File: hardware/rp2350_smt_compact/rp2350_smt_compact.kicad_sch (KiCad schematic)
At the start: 21 parts, among them J1 RP2350-Zero_SMT_Castellated(2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, J2 USB-A_Host(Neltron_5075AR-04-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, J3 RP2350-Zero_SMT_Castellated(2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, SW1 SS-12D00G3 SMD SPDT;Mute/GP28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, SW2 SS-12D00G3 SMD SPDT;Filter/GP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, SW3 SS-12D00G3 SMD SPDT;予備/GP27(フ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, SW4 SS-12D00G3 SMD SPDT;VBUS手動遮断(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, SW5 SS-12D00G3 SMD SPDT;サステイン/J3 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, SW6 PTS645 SMD 6x6 Tact;リセット/J3 G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, U1 TPS2051BDBVR_SOT23-5, U2 USBLC6-2SC6_SOT23-6_USB-A_ESD, U3 USBLC6-2SC6_SOT23-6_USB-C_fut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

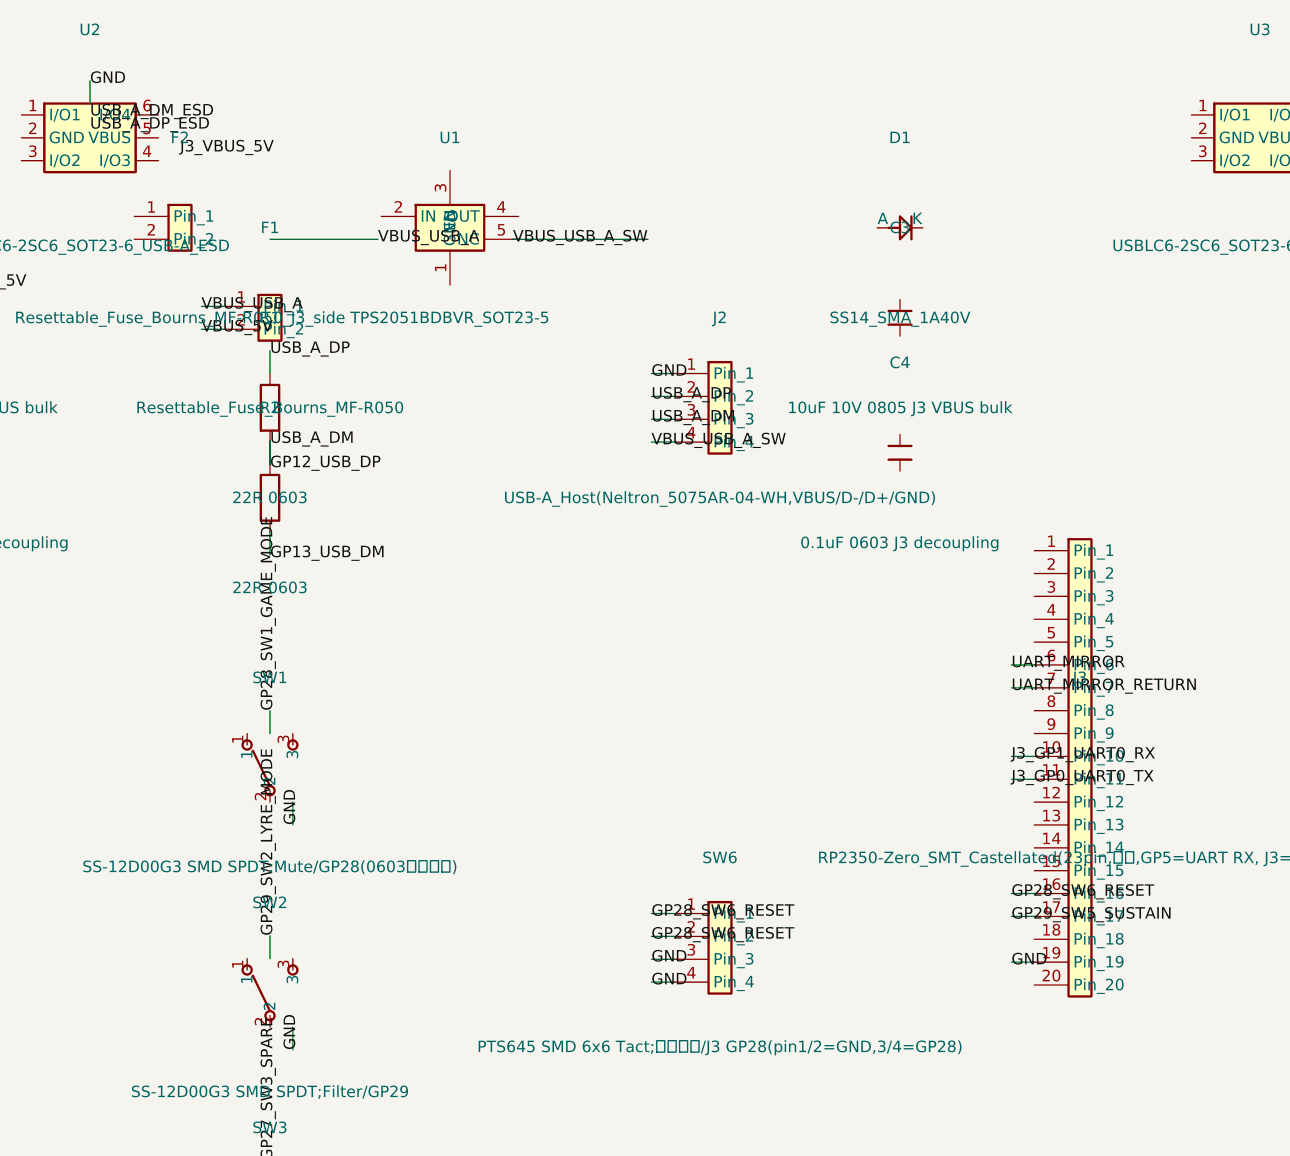
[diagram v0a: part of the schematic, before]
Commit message: review: fix SMT compact carrier inconsistencies
- kicad_pcb: R1/R2 を THT axial (through_hole, P10.16mm, drill0.8) から SMD 0603 (0.9x1.0mm, smd, gap0.8) に修正。pretty の R_0603 と一致、JLC Basic 手ハンダ可能パッケージに準拠。BOM 誤記 C25804(10k) を正しい 22Ω 0603 C22902 に整合
- kicad_pcb: J1/J3 を through_hole 円パッドから RP2350_Zero_SMT_23p_Castellated の正規 smd 矩形+NPTH 半穴定義 (attr smd) に置換。pretty と一致し Castellated Holes 指定を正しく表現。J3 5V を J3_VBUS_5V ネットに接続
- kicad_pcb: SW1-SW5 を THT 3pin (through_hole) から SMスライド SS-12D00G3 SMD 5pad ガルウィング (attr smd, 1.2x1.5mm, anchor 4/5 追加) に置換、SW6 を THT 4pin から PTS645 SMD 6x6 (4pad gull-wing) に置換。pretty と整合
- kicad_pcb: U1 TPS2051B SOT23-5 の未接続パッドにネット割当 (1=GND,2=VBUS_USB_A,3=GND(EN pull-down),4=VBUS_USB_A_SW)。D1/F2/C1-C4 の VBUS/GND ネットも補完
- kicad_sch: U1 EN と GND ピンの浮きを解消 (GND ラベルへ配線)、J3 5V→F2→D1 系と C3/C4 のデカップリングのラベル配線を追加 (いずれもホットプラグ突入対策)。U1 IN=VBUS_USB_A(F1後), OUT=VBUS_USB_A_SW(J2) の既定経路は変更なし
- pretty: 未使用 THT フットプリント 4種 (R_Axial_THT_P10.16mm, SW_SPDT_NKK_115643_Slide, SW_TACT_Akizuki_DTS63, RP2350_Zero_Header_23p) を削除。SMT試作の冗長性解消。残り13種は全て SMD/手ハンダ可能のみ
- bom.csv: R1/R2 の LCSC 誤記修正と備考追記

Edge.Cuts 50x35mm, 2チップ縦並び, 既存 carrier 非破壊, fp-lib-table 整合, USB4105 将来 QFN 言及は維持
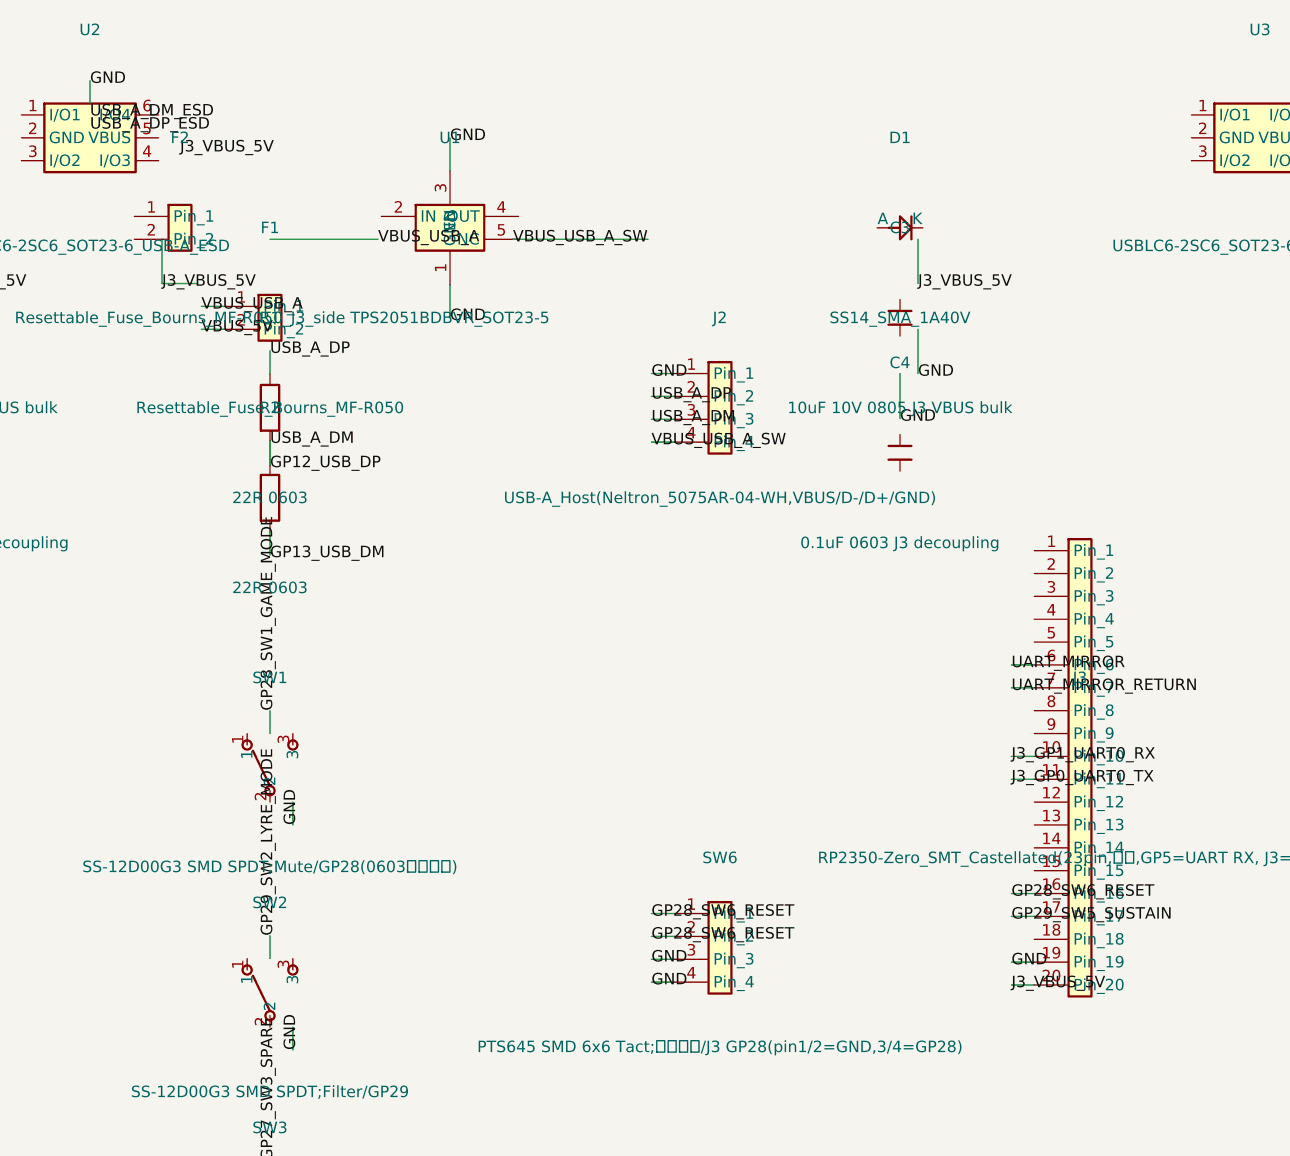
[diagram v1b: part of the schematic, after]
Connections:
- net GND: now also U1.1 (GND), U1.3 (EN)
- net J3_VBUS_5V: now also J3.20 (Pin_20)
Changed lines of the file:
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@@
   (label "USB_A_DP_ESD" (at 90 58.73 0) (effects (font (size 1.27 1.27)) (justify left)))
   (label "USB_A_DM_ESD" (at 90 57.27 0) (effects (font (size 1.27 1.27)) (justify left)))
+  (wire (pts (xy 130 76.35) (xy 130 80)) (stroke (width 0) (type default)))
+  (label "GND" (at 130 80 0) (effects (font (size 1.27 1.27)) (justify left)))
+  (wire (pts (xy 130 63.65) (xy 130 60)) (stroke (width 0) (type default)))
+  (label "GND" (at 130 60 0) (effects (font (size 1.27 1.27)) (justify left)))
+  (wire (pts (xy 194.92 154.13) (xy 192.38 154.13)) (stroke (width 0) (type default)))
+  (label "J3_VBUS_5V" (at 192.38 154.13 0) (effects (font (size 1.27 1.27)) (justify left)))
+  (wire (pts (xy 182 76.19) (xy 182 71.27)) (stroke (width 0) (type default)))
+  (label "J3_VBUS_5V" (at 182 76.19 0) (effects (font (size 1.27 1.27)) (justify left)))
+  (wire (pts (xy 182 86.19) (xy 182 81.27)) (stroke (width 0) (type default)))
+  (label "GND" (at 182 86.19 0) (effects (font (size 1.27 1.27)) (justify left)))
+  (wire (pts (xy 180 91.19) (xy 180 86.19)) (stroke (width 0) (type default)))
+  (label "GND" (at 180 91.19 0) (effects (font (size 1.27 1.27)) (justify left)))
+  (wire (pts (xy 98 76.19) (xy 98 71.27)) (stroke (width 0) (type default)))
+  (label "J3_VBUS_5V" (at 98 76.19 0) (effects (font (size 1.27 1.27)) (justify left)))
+  (wire (pts (xy 102 76.19) (xy 98 76.19)) (stroke (width 0) (type default)))
   (sheet_instances
     (path "/" (page "1"))

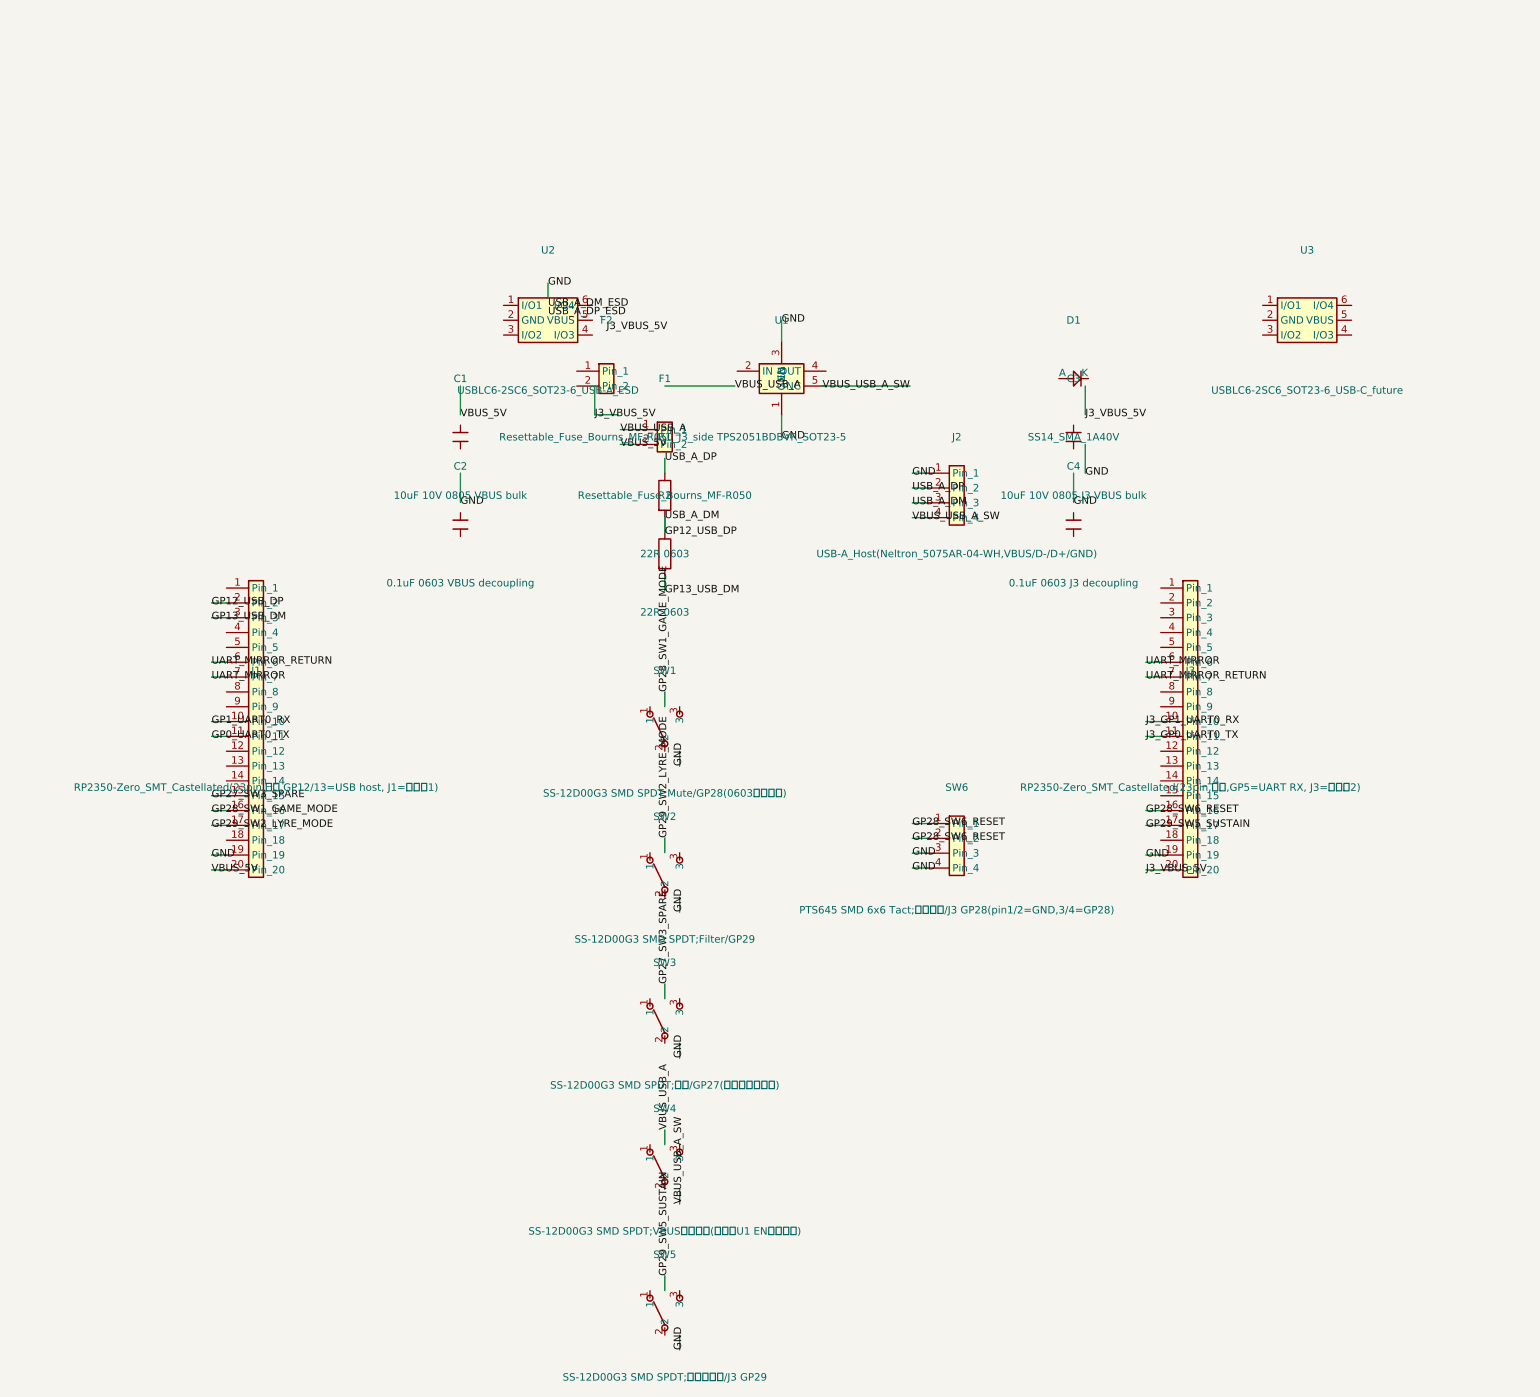
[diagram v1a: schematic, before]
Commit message: docs: kicad_sch清書 & PDF出力、一部pcb調整、配置確認用ドキュメント追加
- kicad_sch清書: 電源(5V→F1→U1 TPS2051B EN=GND→J2 VBUS / J3 5V→F2→D1 SS14)・USB(R1/R2 22R 0603差動90Ω)・ESD(U2/U3 USBLC6)・SW(SS-12D00/PTS645)をグリッド2.54mmに整列、シンボル間10mm以上、Valueを1.0mmフォントで重ならない位置に、ラベルはグローバルラベルで直交配線、重なり0でA4 1枚に収める。テキストで50×35mm構成を注記
- kicad_pcb: 配置確認用で配線除去を維持、Edge.Cuts 50×35mm内で J1(0,6)/J3(0,-6 180°)縦並び中心、J2(0,-14.2)底辺中央、U1(-4,-12.5)/D1(4,-12.5)とC1-4(-7/-3/3/7,-10)をVBUS沿い等間隔、SW1-4右側(16,9/4/-1/-6)・SW5/6左側(-16,-4/-16,9)等間隔、H1-4四隅、TP1(-14,0)中央でHと0.5mmクリアランス確保。シルクRefは読める位置、courtyard重なり0・はみ出し0をDRCで確認(残377件は配線未接続と半穴マスク起因で配置起因は0)
- PDF生成: kicad-cli sch export pdf → docs/smt_compact_sch.pdf(111K)、pcb export pdf(F.Cu/B.Cu/F.SilkS/B.SilkS/Edge.Cuts) → docs/smt_compact_pcb.pdf(36K)、pcb render top/3d → docs/smt_compact_top.png(59K)/smt_compact_3d.png(203K)
- 生成PDF/PNGを docs/ にコミットし FilesパネルからDL可能に
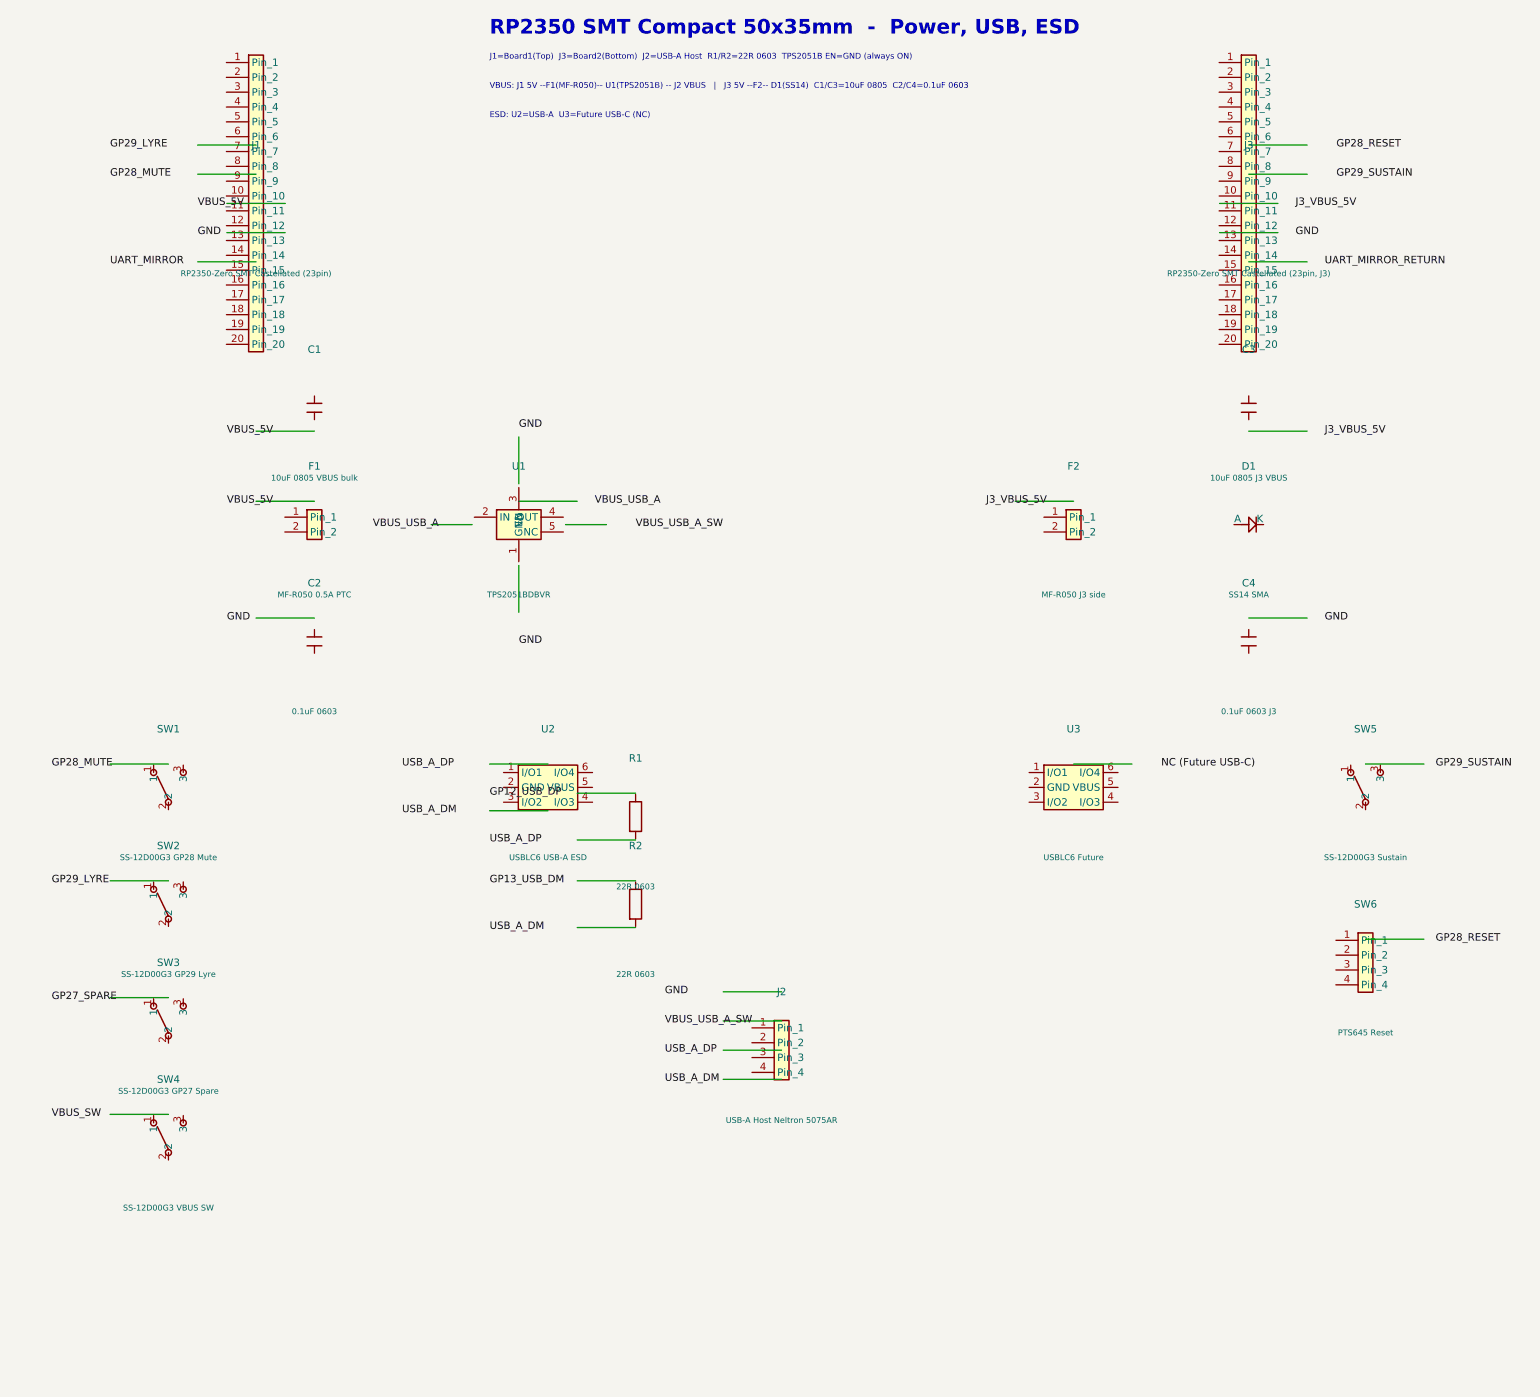
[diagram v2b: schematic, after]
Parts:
- C1: value 10uF 10V 0805 VBUS bulk -> 10uF 0805 VBUS bulk
- C2: value 0.1uF 0603 VBUS decoupling -> 0.1uF 0603
- C3: value 10uF 10V 0805 J3 VBUS bulk -> 10uF 0805 J3 VBUS
- C4: value 0.1uF 0603 J3 decoupling -> 0.1uF 0603 J3
- D1: value SS14_SMA_1A40V -> SS14 SMA
- F1: value Resettable_Fuse_Bourns_MF-R050 -> MF-R050 0.5A PTC
- F2: value Resettable_Fuse_Bourns_MF-R050_J3_side -> MF-R050 J3 side
- J1: value RP2350-Zero_SMT_Castellated(23pin,半穴,GP12/13=USB host, J1=ボード1) -> RP2350-Zero SMT Castellated (23pin)
- J2: value USB-A_Host(Neltron_5075AR-04-WH,VBUS/D-/D+/GND) -> USB-A Host Neltron 5075AR
- J3: value RP2350-Zero_SMT_Castellated(23pin,半穴,GP5=UART RX, J3=ボード2) -> RP2350-Zero SMT Castellated (23pin, J3)
- SW1: value SS-12D00G3 SMD SPDT;Mute/GP28(0603手ハンダ) -> SS-12D00G3 GP28 Mute
- SW2: value SS-12D00G3 SMD SPDT;Filter/GP29 -> SS-12D00G3 GP29 Lyre
- SW3: value SS-12D00G3 SMD SPDT;予備/GP27(ファーム未対応) -> SS-12D00G3 GP27 Spare
- SW4: value SS-12D00G3 SMD SPDT;VBUS手動遮断(将来はU1 ENで代替可) -> SS-12D00G3 VBUS SW
- SW5: value SS-12D00G3 SMD SPDT;サステイン/J3 GP29 -> SS-12D00G3 Sustain
- SW6: value PTS645 SMD 6x6 Tact;リセット/J3 GP28(pin1/2=GND,3/4=GP28) -> PTS645 Reset
- U1: value TPS2051BDBVR_SOT23-5 -> TPS2051BDBVR
- U2: value USBLC6-2SC6_SOT23-6_USB-A_ESD -> USBLC6 USB-A ESD
- U3: value USBLC6-2SC6_SOT23-6_USB-C_future -> USBLC6 Future
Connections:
- net GND: no longer J1.19 (Pin_19), J2.1 (Pin_1), J3.19 (Pin_19), SW6.3 (Pin_3), SW6.4 (Pin_4), U1.1 (GND), U1.3 (EN)
- net GP12_USB_DP: no longer J1.2 (Pin_2), J2.3 (Pin_3), R1.2, R2.1
- net GP13_USB_DM: no longer J1.3 (Pin_3), R2.2
- net J3_VBUS_5V: no longer J3.20 (Pin_20)
- net UART_MIRROR: no longer J1.7 (Pin_7), J3.6 (Pin_6)
- net UART_MIRROR_RETURN: no longer J1.6 (Pin_6), J3.7 (Pin_7)
- net USB_A_DP: no longer J2.2 (Pin_2), R1.1
- net VBUS_5V: no longer F1.2 (Pin_2), J1.20 (Pin_20)
- net VBUS_USB_A: no longer F1.1 (Pin_1)
- net VBUS_USB_A_SW: no longer J2.4 (Pin_4)
- net GP0_UART0_TX: no longer names the net of J1.11 (Pin_11)
- net GP1_UART0_RX: no longer names the net of J1.10 (Pin_10)
- net GP27_SW3_SPARE: no longer names the net of J1.15 (Pin_15)
- net GP28_SW1_GAME_MODE: no longer names the net of J1.16 (Pin_16)
- removed net GP28_SW6_RESET: J3.16 (Pin_16), SW6.1 (Pin_1), SW6.2 (Pin_2)
- net GP29_SW2_LYRE_MODE: no longer names the net of J1.17 (Pin_17)
- net GP29_SW5_SUSTAIN: no longer names the net of J3.17 (Pin_17)
- net J3_GP0_UART0_TX: no longer names the net of J3.11 (Pin_11)
- net J3_GP1_UART0_RX: no longer names the net of J3.10 (Pin_10)
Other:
- note added: "ESD: U2=USB-A U3=Future USB-C (NC)"
- note added: "J1=Board1(Top) J3=Board2(Bottom) J2=USB-A Host R1/R2=22R 0603 TPS2051B EN=GND (always ON)"
- note added: "RP2350 SMT Compact 50x35mm - Power, USB, ESD"
- note added: "VBUS: J1 5V --F1(MF-R050)-- U1(TPS2051B) -- J2 VBUS | J3 5V --F2-- D1(SS14) C1/C3=10uF 0805 C2/C4=0.1uF 0603"
